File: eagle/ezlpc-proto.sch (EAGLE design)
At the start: 61 parts, among them J1 MICRO USB, Q1 12Mhz, T1 MMBT3906, U1 PRTR5V0U2X, U2 MIC5225-3.3v, U3 LPC11U35FHI33/501

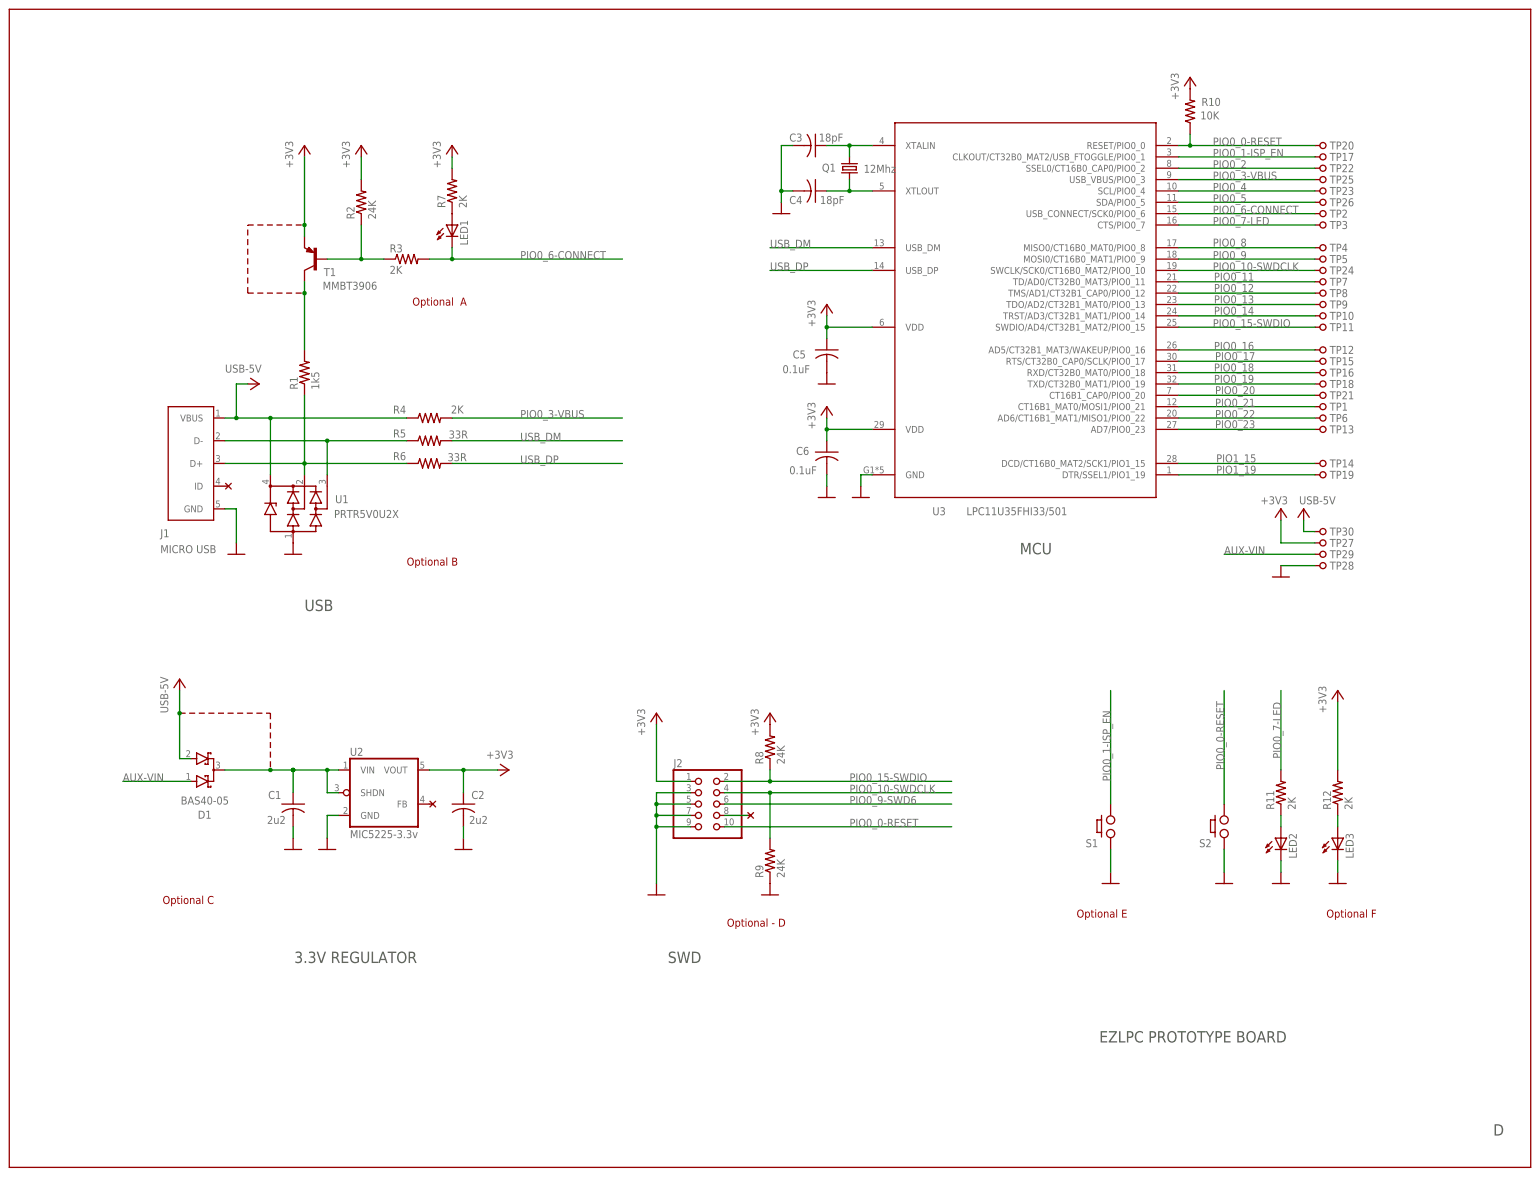
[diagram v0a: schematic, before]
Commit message: Added BOM.
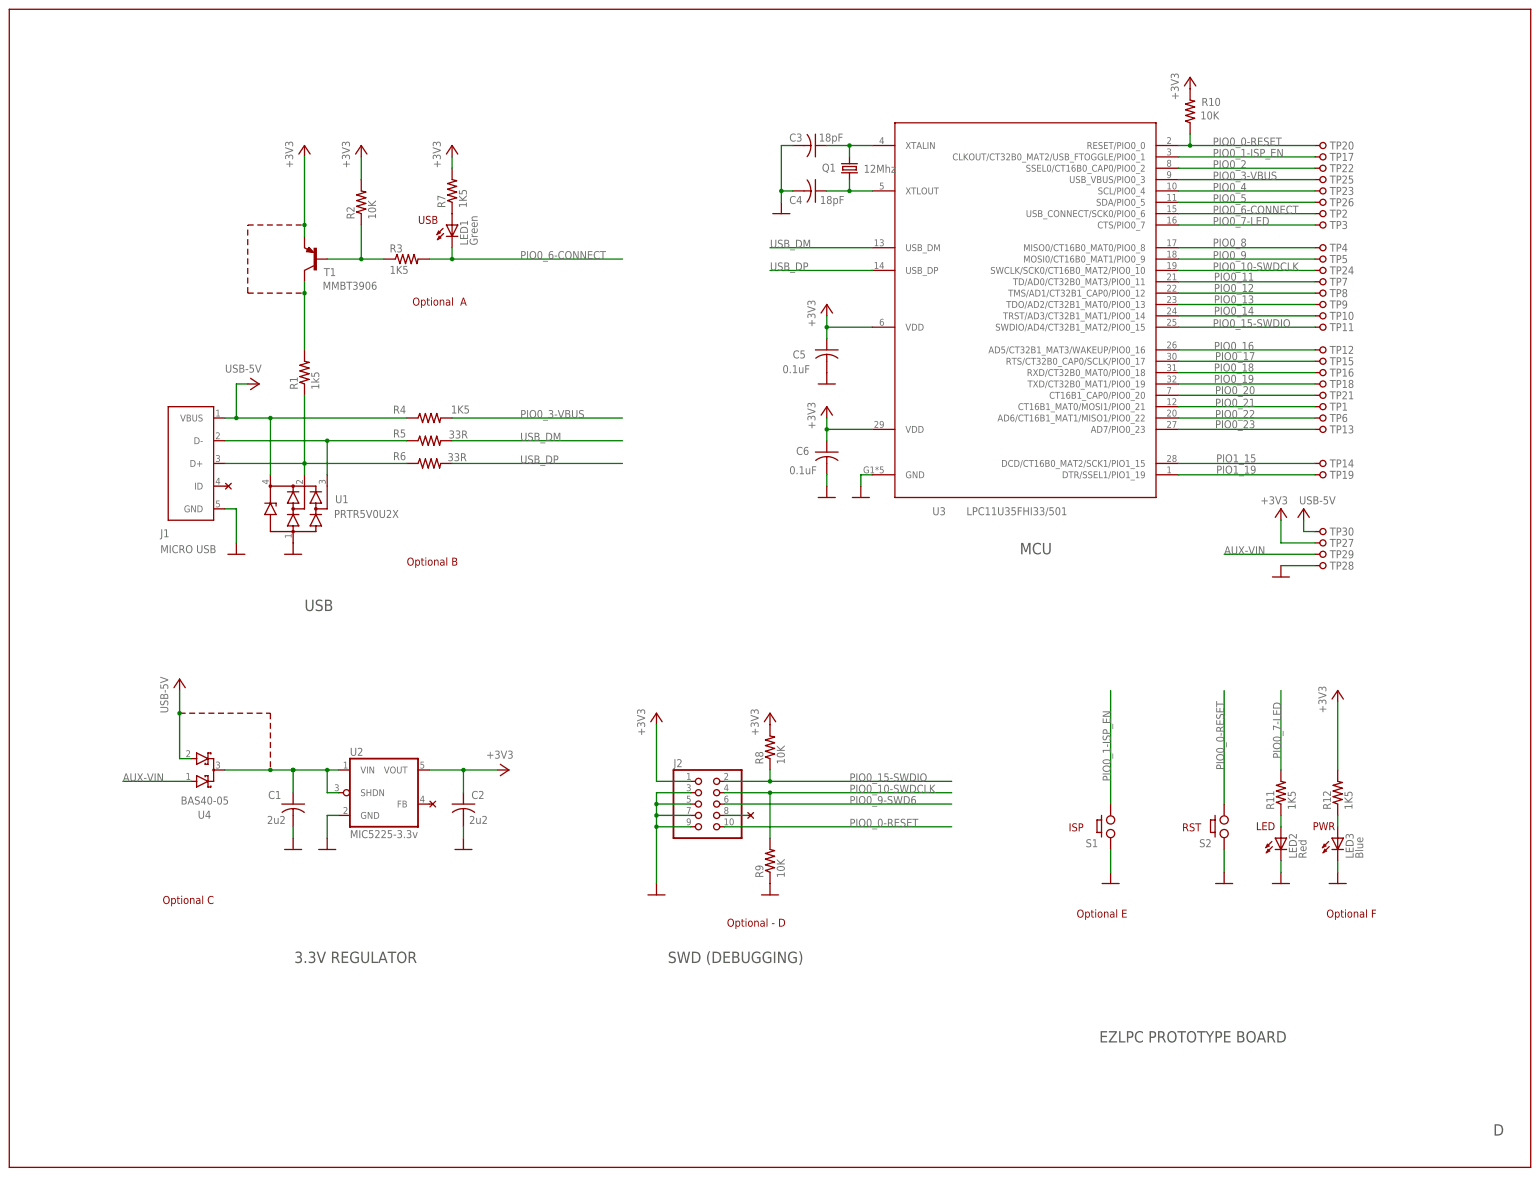
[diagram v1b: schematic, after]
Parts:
- LED1: value (none) -> Green
- LED2: value (none) -> Red
- LED3: value (none) -> Blue
- R11, R12, R3, R4, R7: value 2K -> 1K5
- R2, R8, R9: value 24K -> 10K
- renumbered D1 to U4
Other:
- note added: "ISP"
- note added: "LED"
- note added: "PWR"
- note added: "RST"
- note added: "SWD (DEBUGGING)"
- note removed: "SWD"
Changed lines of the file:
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@@
 <part name="+3V6" library="ezlpc-proto" deviceset="+3V3" device=""/>
 <part name="GND12" library="ezlpc-proto" deviceset="GND" device=""/>
-<part name="R8" library="ezlpc-proto" deviceset="R-US_" device="R0402" value="24K"/>
-<part name="R9" library="ezlpc-proto" deviceset="R-US_" device="R0402" value="24K"/>
+<part name="R8" library="ezlpc-proto" deviceset="R-US_" device="R0402" value="10K"/>
+<part name="R9" library="ezlpc-proto" deviceset="R-US_" device="R0402" value="10K"/>
 <part name="GND13" library="ezlpc-proto" deviceset="GND" device=""/>
 <part name="+3V7" library="ezlpc-proto" deviceset="+3V3" device=""/>
@@
 <part name="S2" library="ezlpc-proto" deviceset="PUSH_BUTTON" device=""/>
 <part name="GND14" library="ezlpc-proto" deviceset="GND" device=""/>
-<part name="R4" library="ezlpc-proto" deviceset="R-US_" device="R0402" value="2K"/>
+<part name="R4" library="ezlpc-proto" deviceset="R-US_" device="R0402" value="1K5"/>
 <part name="+3V9" library="ezlpc-proto" deviceset="+3V3" device=""/>
-<part name="R2" library="ezlpc-proto" deviceset="R-US_" device="R0402" value="24K"/>
+<part name="R2" library="ezlpc-proto" deviceset="R-US_" device="R0402" value="10K"/>
 <part name="+3V10" library="ezlpc-proto" deviceset="+3V3" device=""/>
-<part name="R3" library="ezlpc-proto" deviceset="R-US_" device="R0402" value="2K"/>
-<part name="LED3" library="ezlpc-proto" deviceset="LED" device="CHIP-LED0603"/>
-<part name="R12" library="ezlpc-proto" deviceset="R-US_" device="R0402" value="2K"/>
+<part name="R3" library="ezlpc-proto" deviceset="R-US_" device="R0402" value="1K5"/>
+<part name="LED3" library="ezlpc-proto" deviceset="LED" device="CHIP-LED0603" value="Blue"/>
+<part name="R12" library="ezlpc-proto" deviceset="R-US_" device="R0402" value="1K5"/>
 <part name="GND5" library="ezlpc-proto" deviceset="GND" device=""/>
-<part name="R11" library="ezlpc-proto" deviceset="R-US_" device="R0402" value="2K"/>
-<part name="R7" library="ezlpc-proto" deviceset="R-US_" device="R0402" value="2K"/>
-<part name="LED2" library="ezlpc-proto" deviceset="LED" device="CHIP-LED0603"/>
-<part name="LED1" library="ezlpc-proto" deviceset="LED" device="CHIP-LED0603"/>
+<part name="R11" library="ezlpc-proto" deviceset="R-US_" device="R0402" value="1K5"/>
+<part name="R7" library="ezlpc-proto" deviceset="R-US_" device="R0402" value="1K5"/>
+<part name="LED2" library="ezlpc-proto" deviceset="LED" device="CHIP-LED0603" value="Red"/>
+<part name="LED1" library="ezlpc-proto" deviceset="LED" device="CHIP-LED0603" value="Green"/>
 <part name="GND6" library="ezlpc-proto" deviceset="GND" device=""/>
 <part name="+3V4" library="ezlpc-proto" deviceset="+3V3" device=""/>
@@
 <part name="R6" library="ezlpc-proto" deviceset="R-US_" device="R0402" value="33R"/>
 <part name="R5" library="ezlpc-proto" deviceset="R-US_" device="R0402" value="33R"/>
-<part name="D1" library="ezlpc-proto" deviceset="BAS40-05" device=""/>
+<part name="U4" library="ezlpc-proto" deviceset="BAS40-05" device=""/>
 <part name="P+1" library="ezlpc-proto" deviceset="USB-5V" device=""/>
 <part name="TP20" library="ezlpc-proto" deviceset="PINHD-1X1" device=""/>
@@
 </polygon>
 <text x="66.04" y="124.46" size="2.54" layer="97">USB</text>
-<text x="147.32" y="45.72" size="2.54" layer="97">SWD</text>
+<text x="147.32" y="45.72" size="2.54" layer="97">SWD (DEBUGGING)</text>
 <polygon width="0.1524" layer="98">
 <vertex x="17.78" y="96.52"/>
@@
 </polygon>
 <text x="294.64" y="55.88" size="1.778" layer="94">Optional F</text>
+<text x="236.982" y="75.184" size="1.778" layer="94">ISP</text>
+<text x="262.382" y="75.184" size="1.778" layer="94">RST</text>
+<text x="278.892" y="75.438" size="1.778" layer="94">LED</text>
+<text x="291.592" y="75.438" size="1.778" layer="94">PWR</text>
+<text x="91.44" y="211.074" size="1.778" layer="94">USB</text>
 </plain>
 <instances>
@@
 <attribute name="VALUE" x="98.298" y="163.068" size="1.778" layer="96"/>
 </instance>
-<instance part="D1" gate="G$1" x="43.18" y="88.9" smashed="yes" rot="MR180">
+<instance part="U4" gate="G$1" x="43.18" y="88.9" smashed="yes" rot="MR180">
 <attribute name="NAME" x="42.164" y="79.7814" size="1.778" layer="95" rot="MR180"/>
 <attribute name="VALUE" x="38.354" y="82.9564" size="1.778" layer="96" rot="MR180"/>
@@
 </segment>
 <segment>
-<pinref part="D1" gate="G$1" pin="A2"/>
+<pinref part="U4" gate="G$1" pin="A2"/>
 <wire x1="40.64" y1="91.44" x2="38.1" y2="91.44" width="0.1524" layer="91"/>
 <wire x1="38.1" y1="91.44" x2="38.1" y2="101.6" width="0.1524" layer="91"/>
@@
 <pinref part="C1" gate="G$1" pin="1"/>
 <wire x1="63.5" y1="83.82" x2="63.5" y2="88.9" width="0.1524" layer="91"/>
-<pinref part="D1" gate="G$1" pin="C"/>
+<pinref part="U4" gate="G$1" pin="C"/>
 <junction x="63.5" y="88.9"/>
 <junction x="63.5" y="88.9"/>
@@
 </segment>
 <segment>
-<pinref part="D1" gate="G$1" pin="A1"/>
+<pinref part="U4" gate="G$1" pin="A1"/>
 <wire x1="40.64" y1="86.36" x2="25.4" y2="86.36" width="0.1524" layer="91"/>
 <label x="25.4" y="86.36" size="1.778" layer="95"/>

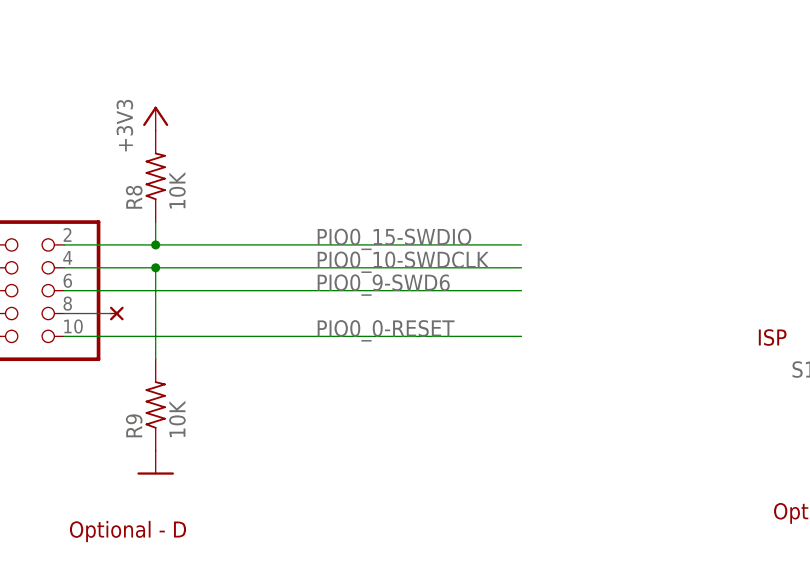
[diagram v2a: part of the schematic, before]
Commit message: Minor net rename.
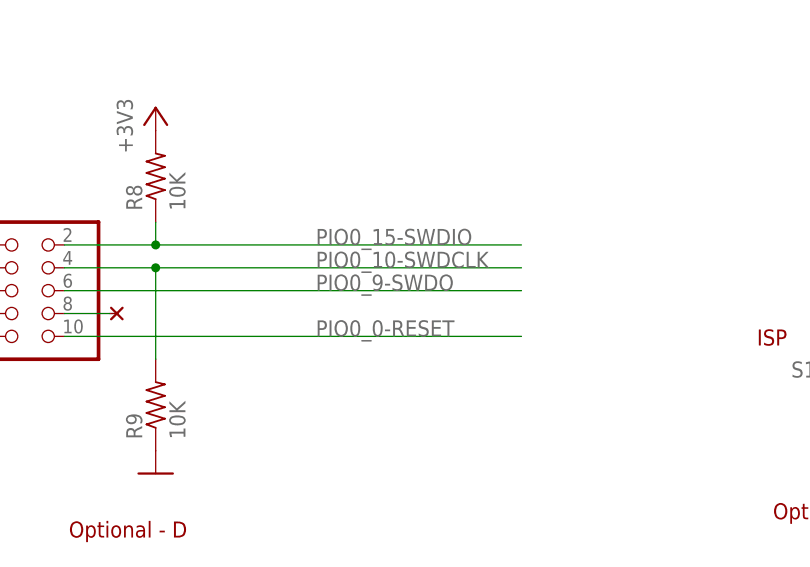
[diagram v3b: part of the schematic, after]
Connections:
- net PIO0_9-SWD6 renamed PIO0_9-SWDO
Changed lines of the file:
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@@
 </segment>
 </net>
-<net name="PIO0_9-SWD6" class="0">
+<net name="PIO0_9-SWDO" class="0">
 <segment>
 <pinref part="J2" gate="A" pin="6"/>
